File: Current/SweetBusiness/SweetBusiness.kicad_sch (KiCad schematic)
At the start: 57 parts, among them J2 I2C, J4 USB, U0 RP2040, U1 MT2492, U2 W25Q128JVS, U3 USBLC6-2SC6, Y0 CSTCE12M0G55-R0

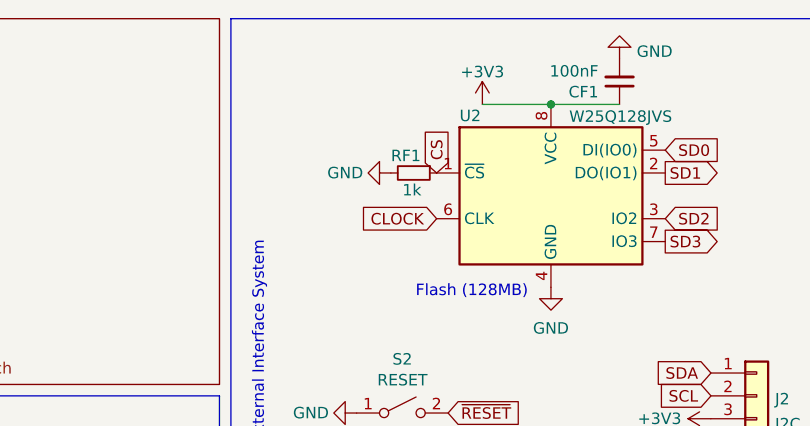
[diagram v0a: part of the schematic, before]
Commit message: Fixed the goddamned power system.
and it works now on sb6
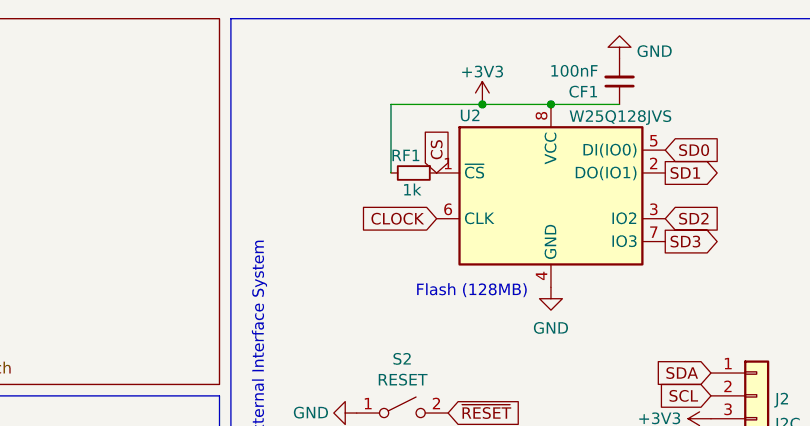
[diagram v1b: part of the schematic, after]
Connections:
- net +3V3: now also RF1.2
- net GND: no longer RF1.2
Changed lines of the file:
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@@
   (junction (at 66.04 182.88) (diameter 0) (color 0 0 0 0)
+  )
+  (junction (at 226.06 22.86) (diameter 0) (color 0 0 0 0)
   )
   (junction (at 48.26 116.84) (diameter 0) (color 0 0 0 0)
@@
     (stroke (width 0) (type default))
   )
+  (wire (pts (xy 215.9 22.86) (xy 226.06 22.86))
+    (stroke (width 0) (type default))
+  )
   (polyline (pts (xy 15.24 202.565) (xy 152.4 202.565))
     (stroke (width 0) (type default))
@@
   )
   (polyline (pts (xy 198.12 13.335) (xy 265.43 13.335))
+    (stroke (width 0) (type default))
+  )
+  (wire (pts (xy 215.9 30.48) (xy 215.9 22.86))
     (stroke (width 0) (type default))
   )
@@
         )
       )
-    )
-  )
-  (symbol (lib_id "power:GND") (at 215.9 30.48 270) (unit 1)
-    (in_bom yes) (on_board yes) (dnp no)
-    (property "Reference" "#PWR0129" (at 209.55 30.48 0)
-      (effects (font (size 1.27 1.27)) hide)
-    )
-    (property "Value" "GND" (at 210.82 30.48 90)
-      (effects (font (size 1.27 1.27)))
-    )
-    (property "Footprint" "" (at 215.9 30.48 0)
-      (effects (font (size 1.27 1.27)) hide)
-    )
-    (property "Datasheet" "" (at 215.9 30.48 0)
-      (effects (font (size 1.27 1.27)) hide)
-    )
-    (pin "1")
-    (instances
-      (project "SweetBusiness"
-        (path "/20c315f4-1e4f-49aa-8d61-778a7389df7e"
-          (reference "#PWR0129") (unit 1)
-        )
-      )

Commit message: Firmware backup added.
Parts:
- LP1: LCSC C44893 -> C5189958
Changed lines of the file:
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@@
       (effects (font (size 1.27 1.27)) hide)
     )
-    (property "LCSC" "C44893" (at 99.06 176.53 90)
+    (property "LCSC" "C5189958" (at 99.06 176.53 90)
       (effects (font (size 1.27 1.27)) hide)
     )
